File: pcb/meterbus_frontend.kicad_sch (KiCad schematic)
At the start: 38 parts, among them Q2 AO3400A, U10 AMS1117-5.0, U2 SN74HC132DR, U3 ISO6721RBDR

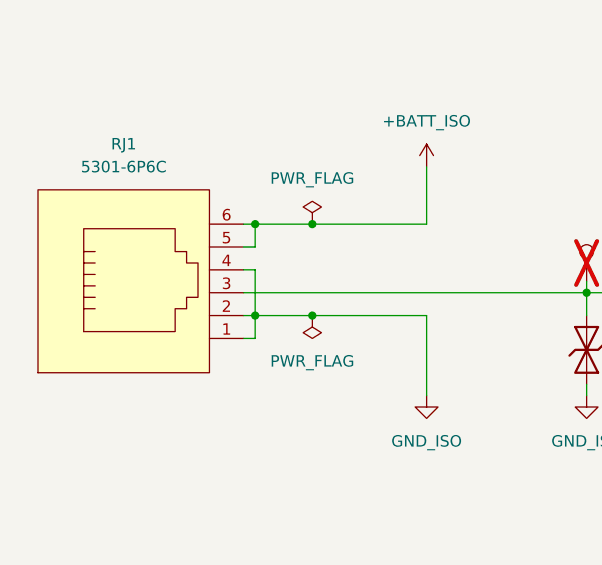
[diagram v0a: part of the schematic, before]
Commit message: pcb: update symbols and footprints to fix drc
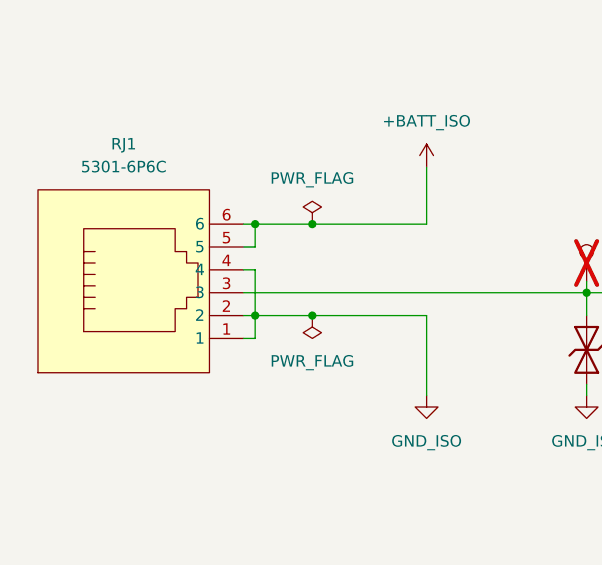
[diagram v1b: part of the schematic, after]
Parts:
- C1: Price 0.035USD -> 0.061USD; Stock 3698334 -> 1900877
- C3, C35, C5, C6, C7: Stock 70324515 -> 37493696
- C4: Price 0.021USD -> 0.020USD; Stock 3388297 -> 3475471
- D10, D11: footprint PCM_JLCPCB:D_SMA -> PCM_JLCPCB:D_DO-214AC(SMA); Price 0.038USD -> 0.039USD; Stock 103246 -> 77690
- D4: Stock 2976925 -> 5618781
- D5: Price 0.029USD -> 0.030USD; Stock 272493 -> 1058068
- D6: Price 0.014USD -> 0.018USD; Stock 2062782 -> 2234536
- Q2: Price 0.074USD -> 0.079USD; Stock 463122 -> 1814497
- R1, R5: Price 0.004USD -> 0.005USD; Stock 8202320 -> 9270288
- R10, R9: Price 0.004USD -> 0.005USD; Stock 51181774 -> 22319909
- R2: Price 0.004USD -> 0.005USD; Stock 3961571 -> 4092207
- R3, R7: Price 0.004USD -> 0.005USD; Stock 7820113 -> 10814547
- R4: Stock 331035 -> 723877
- R6, R8: Price 0.004USD -> 0.005USD; Stock 2977706 -> 3511720
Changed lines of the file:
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@@
 			)
 		)
-		(property "Stock" "8202320"
+		(property "Stock" "9270288"
 			(at 100.33 88.9 0)
 			(hide yes)
@@
 			)
 		)
-		(property "Price" "0.004USD"
+		(property "Price" "0.005USD"
 			(at 100.33 88.9 0)
 			(hide yes)
@@
 			)
 		)
-		(property "Stock" "2977706"
+		(property "Stock" "3511720"
 			(at 124.46 105.41 0)
 			(hide yes)
@@
 			)
 		)
-		(property "Price" "0.004USD"
+		(property "Price" "0.005USD"
 			(at 124.46 105.41 0)
 			(hide yes)
@@
 			)
 		)
-		(property "Stock" "7820113"
+		(property "Stock" "10814547"
 			(at 179.07 50.8 0)
 			(hide yes)
@@
 			)
 		)
-		(property "Price" "0.004USD"
+		(property "Price" "0.005USD"
 			(at 179.07 50.8 0)
 			(hide yes)
@@
 			)
 		)
-		(property "Description" "50V 10uF X5R ±10% 1206 Multilayer Ceramic Capacitors MLCC - SMD/SMT ROHS"
+		(property "Description" "10uF 50V X5R ±10% 1206 Multilayer Ceramic Capacitors MLCC - SMD/SMT ROHS"
 			(at 57.15 175.26 0)
 			(hide yes)
@@
 			)
 		)
-		(property "Stock" "3698334"
+		(property "Stock" "1900877"
 			(at 57.15 175.26 0)
 			(hide yes)
@@
 			)
 		)
-		(property "Price" "0.035USD"
+		(property "Price" "0.061USD"
 			(at 57.15 175.26 0)
 			(hide yes)
@@
 			)
 		)
-		(property "Description" "30V 5.7A 26.5mΩ@10V,5.7A 1.4W 1.5V@250uA 1 N-Channel SOT-23-3L MOSFETs ROHS"
+		(property "Description" "-55°C~+150°C 1 N-channel 1.45V 1.4W 30V 48mΩ@2.5V 5.7A 50pF 630pF 75pF 7nC@10V N-Channel SOT-23 MOSFETs ROHS"
 			(at 102.87 99.06 0)
 			(hide yes)
@@
 			)
 		)
-		(property "Stock" "463122"
+		(property "Stock" "1814497"
 			(at 102.87 99.06 0)
 			(hide yes)
@@
 			)
 		)
-		(property "Price" "0.074USD"
+		(property "Price" "0.079USD"
 			(at 102.87 99.06 0)
 			(hide yes)
@@
 			)
 		)
-		(property "Stock" "70324515"
+		(property "Stock" "37493696"
 			(at 195.58 38.1 0)
 			(hide yes)
@@
 			)
 		)
-		(property "Stock" "2976925"
+		(property "Stock" "5618781"
 			(at 124.46 114.3 0)
 			(hide yes)
@@
 			)
 		)
-		(property "Stock" "70324515"
+		(property "Stock" "37493696"
 			(at 242.57 43.18 0)
 			(hide yes)
@@
 			)
 		)
-		(property "Description" "50V 100nF X7R ±10% 0603 Multilayer Ceramic Capacitors MLCC - SMD/SMT ROHS"
+		(property "Description" "100nF 50V X7R ±10% 0603 Multilayer Ceramic Capacitors MLCC - SMD/SMT ROHS"
 			(at 106.68 175.26 0)
 			(hide yes)
@@
 			)
 		)
-		(property "Stock" "70324515"
+		(property "Stock" "37493696"
 			(at 106.68 175.26 0)
 			(hide yes)
@@
 			)
 		)
-		(property "Footprint" "PCM_JLCPCB:D_SMA"
+		(property "Footprint" "PCM_JLCPCB:D_DO-214AC(SMA)"
 			(at 83.312 62.23 90)
 			(hide yes)
@@
 			)
 		)
-		(property "Description" "8.8A 45.4V 400W 34.4V Bidirectional 28V SMA ESD and Surge Protection (TVS/ESD) ROHS"
+		(property "Description" "-55°C~+150°C 1uA 28V 34.4V 400W@10/1000us 45.4V 8.8A Bidirectional IEC 61000-4-2 TVS DO-214AC(SMA) ESD and Surge Protection (TVS/ESD) ROHS"
 			(at 85.09 62.23 0)
 			(hide yes)
@@
 			)
 		)
-		(property "Stock" "103246"
+		(property "Stock" "77690"
 			(at 85.09 62.23 0)
 			(hide yes)
@@
 			)
 		)
-		(property "Price" "0.038USD"
+		(property "Price" "0.039USD"
 			(at 85.09 62.23 0)
 			(hide yes)
@@
 			)
 		)
-		(property "Footprint" "PCM_JLCPCB:D_SMA"
+		(property "Footprint" "PCM_JLCPCB:D_DO-214AC(SMA)"
 			(at 26.162 175.26 90)
 			(hide yes)
@@
 			)
 		)
-		(property "Description" "8.8A 45.4V 400W 34.4V Bidirectional 28V SMA ESD and Surge Protection (TVS/ESD) ROHS"
+		(property "Description" "-55°C~+150°C 1uA 28V 34.4V 400W@10/1000us 45.4V 8.8A Bidirectional IEC 61000-4-2 TVS DO-214AC(SMA) ESD and Surge Protection (TVS/ESD) ROHS"
 			(at 27.94 175.26 0)
 			(hide yes)
@@
 			)
 		)
-		(property "Stock" "103246"
+		(property "Stock" "77690"
 			(at 27.94 175.26 0)
 			(hide yes)
@@
 			)
 		)
-		(property "Price" "0.038USD"
+		(property "Price" "0.039USD"
 			(at 27.94 175.26 0)
 			(hide yes)
@@
 			)
 		)
-		(property "Stock" "7820113"
+		(property "Stock" "10814547"
 			(at 111.76 105.41 0)
 			(hide yes)
@@
 			)
 		)
-		(property "Price" "0.004USD"
+		(property "Price" "0.005USD"
 			(at 111.76 105.41 0)
 			(hide yes)
@@
 			)
 		)
-		(property "Stock" "2062782"
+		(property "Stock" "2234536"
 			(at 179.07 69.85 0)
 			(hide yes)
@@
 			)
 		)
-		(property "Price" "0.014USD"
+		(property "Price" "0.018USD"
 			(at 179.07 69.85 0)
 			(hide yes)
@@
 			)
 		)
-		(property "Stock" "2977706"
+		(property "Stock" "3511720"
 			(at 179.07 60.96 0)
 			(hide yes)
@@
 			)
 		)
-		(property "Price" "0.004USD"
+		(property "Price" "0.005USD"
 			(at 179.07 60.96 0)
 			(hide yes)
@@
 			)
 		)
-		(property "Stock" "51181774"
+		(property "Stock" "22319909"
 			(at 265.43 49.53 0)
 			(hide yes)
@@
 			)
 		)
-		(property "Price" "0.004USD"
+		(property "Price" "0.005USD"
 			(at 265.43 49.53 0)
 			(hide yes)
@@
 			)
 		)
-		(property "Stock" "70324515"
+		(property "Stock" "37493696"
 			(at 242.57 133.35 0)
 			(hide yes)
@@
 			)
 		)
-		(property "Stock" "3961571"
+		(property "Stock" "4092207"
 			(at 106.68 55.88 0)
 			(hide yes)
@@
 			)
 		)
-		(property "Price" "0.004USD"
+		(property "Price" "0.005USD"
 			(at 106.68 55.88 0)
 			(hide yes)
@@
 			)
 		)
-		(property "Description" "25V 10uF X5R ±20% 0603 Multilayer Ceramic Capacitors MLCC - SMD/SMT ROHS"
+		(property "Description" "10uF 25V X5R ±20% 0603 Multilayer Ceramic Capacitors MLCC - SMD/SMT ROHS"
 			(at 121.92 175.26 0)
 			(hide yes)
@@
 			)
 		)
-		(property "Stock" "3388297"
+		(property "Stock" "3475471"
 			(at 121.92 175.26 0)
 			(hide yes)
@@
 			)
 		)
-		(property "Price" "0.021USD"
+		(property "Price" "0.020USD"
 			(at 121.92 175.26 0)
 			(hide yes)
@@
 			)
 		)
-		(property "Stock" "8202320"
+		(property "Stock" "9270288"
 			(at 119.38 99.06 0)
 			(hide yes)
@@
 			)
 		)
-		(property "Price" "0.004USD"
+		(property "Price" "0.005USD"
 			(at 119.38 99.06 0)
 			(hide yes)
@@
 			)
 		)
-		(property "Stock" "51181774"
+		(property "Stock" "22319909"
 			(at 269.24 49.53 0)
 			(hide yes)
@@
 			)
 		)
-		(property "Price" "0.004USD"
+		(property "Price" "0.005USD"
 			(at 269.24 49.53 0)
 			(hide yes)
@@
 			)
 		)
-		(property "Description" "100V 850mV@2A 2A SMA(DO-214AC) Schottky Diodes ROHS"
+		(property "Description" "-55°C~+150°C 1 Independent 100V 2A 500uA@100V 850mV@2A SMA(DO-214AC) Schottky Diodes ROHS"
 			(at 36.83 170.18 0)
 			(hide yes)
@@
 			)
 		)
-		(property "Stock" "272493"
+		(property "Stock" "1058068"
 			(at 36.83 170.18 0)
 			(hide yes)
@@
 			)
 		)
-		(property "Price" "0.029USD"
+		(property "Price" "0.030USD"
 			(at 36.83 170.18 0)
 			(hide yes)
@@
 			)
 		)
-		(property "Stock" "331035"
+		(property "Stock" "723877"
 			(at 113.03 62.23 0)
 			(hide yes)
@@
 			)
 		)
-		(property "Description" "50V 100nF X7R ±10% 0603 Multilayer Ceramic Capacitors MLCC - SMD/SMT ROHS"
+		(property "Description" "100nF 50V X7R ±10% 0603 Multilayer Ceramic Capacitors MLCC - SMD/SMT ROHS"
 			(at 69.85 175.26 0)
 			(hide yes)
@@
 			)
 		)
-		(property "Stock" "70324515"
+		(property "Stock" "37493696"
 			(at 69.85 175.26 0)
 			(hide yes)
